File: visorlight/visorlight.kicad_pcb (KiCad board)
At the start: 2 copper layers, 85 x 35 mm, 3 parts, among them J1 Conn_01x04

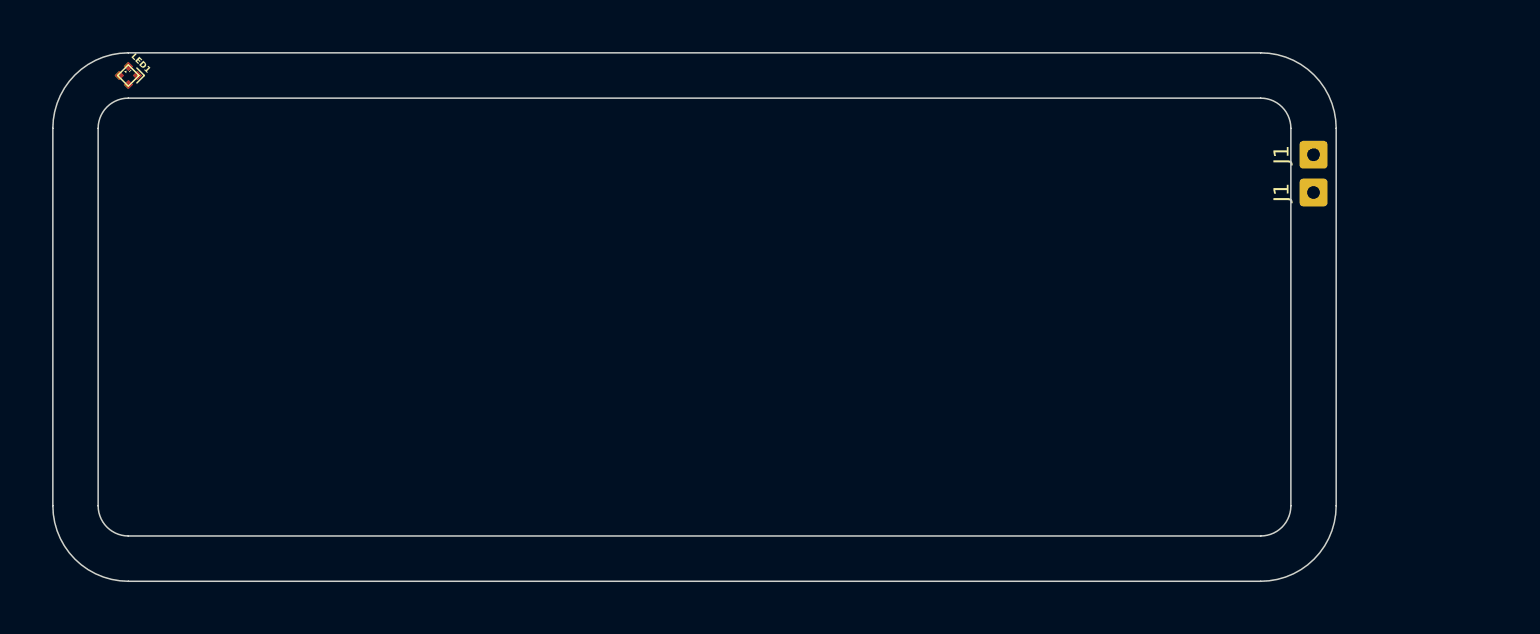
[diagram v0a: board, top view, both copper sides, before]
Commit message: moar leds
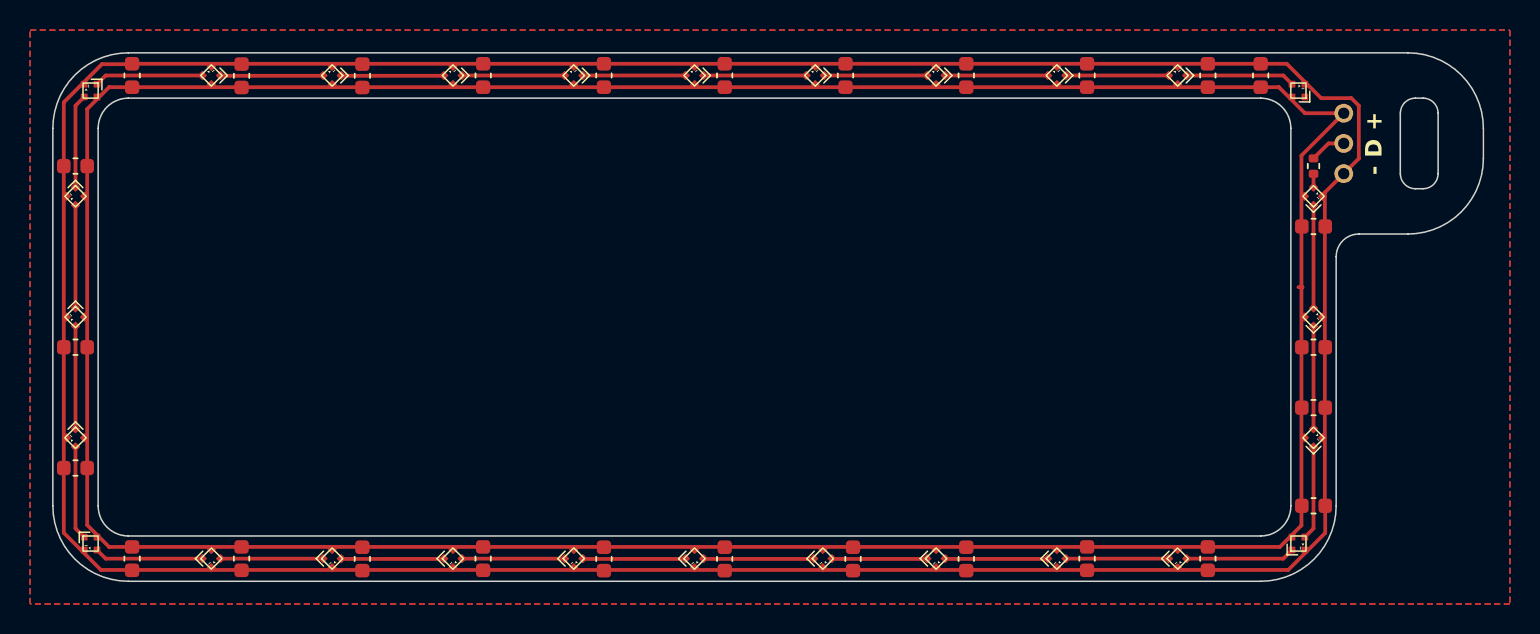
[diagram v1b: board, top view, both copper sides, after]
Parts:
- removed the J1 at (191.0, 89.2)
- removed the J1 at (191.0, 91.8)
- added C1: 0.1µF, Capacitor_SMD:C_0603_1608Metric, F.Cu at (191.0, 94.0)
- added C10: 0.1µF, Capacitor_SMD:C_0603_1608Metric, F.Cu at (144.0, 116.0)
- added C11: 0.1µF, Capacitor_SMD:C_0603_1608Metric, F.Cu at (136.0, 116.0)
- added C12: 0.1µF, Capacitor_SMD:C_0603_1608Metric, F.Cu at (128.0, 116.0)
- added C13: 0.1µF, Capacitor_SMD:C_0603_1608Metric, F.Cu at (120.0, 116.0)
- added C14: 0.1µF, Capacitor_SMD:C_0603_1608Metric, F.Cu at (112.8, 116.0)
- added C15: 0.1µF, Capacitor_SMD:C_0603_1608Metric, F.Cu at (109.0, 110.0)
- added C16: 0.1µF, Capacitor_SMD:C_0603_1608Metric, F.Cu at (109.0, 102.0)
- added C17: 0.1µF, Capacitor_SMD:C_0603_1608Metric, F.Cu at (109.0, 90.0)
- added C18: 0.1µF, Capacitor_SMD:C_0603_1608Metric, F.Cu at (112.8, 84.0)
- added C19: 0.1µF, Capacitor_SMD:C_0603_1608Metric, F.Cu at (120.0, 84.0)
- added C2: 0.1µF, Capacitor_SMD:C_0603_1608Metric, F.Cu at (191.0, 102.0)
- added C20: 0.1µF, Capacitor_SMD:C_0603_1608Metric, F.Cu at (128.0, 84.0)
- added C21: 0.1µF, Capacitor_SMD:C_0603_1608Metric, F.Cu at (136.0, 84.0)
- added C22: 0.1µF, Capacitor_SMD:C_0603_1608Metric, F.Cu at (144.0, 84.0)
- added C23: 0.1µF, Capacitor_SMD:C_0603_1608Metric, F.Cu at (152.0, 84.0)
- added C24: 0.1µF, Capacitor_SMD:C_0603_1608Metric, F.Cu at (160.0, 84.0)
- added C25: 0.1µF, Capacitor_SMD:C_0603_1608Metric, F.Cu at (168.0, 84.0)
- added C26: 0.1µF, Capacitor_SMD:C_0603_1608Metric, F.Cu at (176.0, 84.0)
- added C27: 0.1µF, Capacitor_SMD:C_0603_1608Metric, F.Cu at (184.0, 84.0)
- added C28: 0.1µF, Capacitor_SMD:C_0603_1608Metric, F.Cu at (187.5, 84.0)
- added C3: 0.1µF, Capacitor_SMD:C_0603_1608Metric, F.Cu at (191.0, 106.0)
- added C4: 0.1µF, Capacitor_SMD:C_0603_1608Metric, F.Cu at (191.0, 112.5)
- added C5: 0.1µF, Capacitor_SMD:C_0603_1608Metric, F.Cu at (184.0, 116.0)
- added C6: 0.1µF, Capacitor_SMD:C_0603_1608Metric, F.Cu at (176.0, 116.0)
- added C7: 0.1µF, Capacitor_SMD:C_0603_1608Metric, F.Cu at (168.0, 116.0)
- added C8: 0.1µF, Capacitor_SMD:C_0603_1608Metric, F.Cu at (160.5, 116.0)
- added C9: 0.1µF, Capacitor_SMD:C_0603_1608Metric, F.Cu at (152.0, 116.0)
- added J1: Conn_01x03, visorlight_parts:Wires_3x_Relief, F.Cu at (193.0, 88.5)
- added LED10: ~, visorlight_parts:LED_1010RGBC, F.Cu at (142.0, 116.0)
- added LED11: ~, visorlight_parts:LED_1010RGBC, F.Cu at (134.0, 116.0)
- added LED12: ~, visorlight_parts:LED_1010RGBC, F.Cu at (126.0, 116.0)
- added LED13: ~, visorlight_parts:LED_1010RGBC, F.Cu at (118.0, 116.0)
- added LED14: ~, visorlight_parts:LED_1010RGBC, F.Cu at (110.0, 115.0)
- added LED15: ~, visorlight_parts:LED_1010RGBC, F.Cu at (109.0, 108.0)
- added LED16: ~, visorlight_parts:LED_1010RGBC, F.Cu at (109.0, 100.0)
- added LED17: ~, visorlight_parts:LED_1010RGBC, F.Cu at (109.0, 92.0)
- added LED18: ~, visorlight_parts:LED_1010RGBC, F.Cu at (110.0, 85.0)
- added LED19: ~, visorlight_parts:LED_1010RGBC, F.Cu at (118.0, 84.0)
- added LED2: ~, visorlight_parts:LED_1010RGBC, F.Cu at (191.0, 100.0)
- added LED20: ~, visorlight_parts:LED_1010RGBC, F.Cu at (126.0, 84.0)
- added LED21: ~, visorlight_parts:LED_1010RGBC, F.Cu at (134.0, 84.0)
- added LED22: ~, visorlight_parts:LED_1010RGBC, F.Cu at (142.0, 84.0)
- added LED23: ~, visorlight_parts:LED_1010RGBC, F.Cu at (150.0, 84.0)
- added LED24: ~, visorlight_parts:LED_1010RGBC, F.Cu at (158.0, 84.0)
- added LED25: ~, visorlight_parts:LED_1010RGBC, F.Cu at (166.0, 84.0)
- added LED26: ~, visorlight_parts:LED_1010RGBC, F.Cu at (174.0, 84.0)
- added LED27: ~, visorlight_parts:LED_1010RGBC, F.Cu at (182.0, 84.0)
- added LED28: ~, visorlight_parts:LED_1010RGBC, F.Cu at (190.0, 85.0)
- added LED3: ~, visorlight_parts:LED_1010RGBC, F.Cu at (191.0, 108.0)
- added LED4: ~, visorlight_parts:LED_1010RGBC, F.Cu at (190.0, 115.0)
- added LED5: ~, visorlight_parts:LED_1010RGBC, F.Cu at (182.0, 116.0)
- added LED6: ~, visorlight_parts:LED_1010RGBC, F.Cu at (174.0, 116.0)
- added LED7: ~, visorlight_parts:LED_1010RGBC, F.Cu at (166.0, 116.0)
- added LED8: ~, visorlight_parts:LED_1010RGBC, F.Cu at (158.5, 116.0)
- added LED9: ~, visorlight_parts:LED_1010RGBC, F.Cu at (150.0, 116.0)
- added R1: 100Ω, Resistor_SMD:R_0402_1005Metric, F.Cu at (191.0, 90.0)
- LED1: footprint project_parts:LED_1010RGBC -> visorlight_parts:LED_1010RGBC
- moved LED1 78.9 mm to (191.0, 92.0), turned to 135 degrees
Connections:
- LED1 pad 1: unconnected-(LED1-DO-Pad1) -> Net-(LED1-DO)
- LED1 pad 2: unconnected-(LED1-VDD-Pad2) -> VDD
- LED1 pad 3: unconnected-(LED1-GND-Pad3) -> GND
- LED1 pad 4: unconnected-(LED1-DI-Pad4) -> Net-(LED1-DI)
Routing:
- net GND: track 0.00 -> 231.3 mm
- net VDD: track 0.00 -> 222.7 mm
- net Net-(LED8-DO): track 0.00 -> 7.31 mm
- net Net-(LED18-DO): track 0.00 -> 7.21 mm
- net Net-(LED13-DO): track 0.00 -> 7.21 mm
- net Net-(LED4-DO): track 0.00 -> 7.21 mm
- net Net-(LED27-DO): track 0.00 -> 7.21 mm
- net Net-(LED5-DO): track 0.00 -> 6.83 mm
- net Net-(LED21-DO): track 0.00 -> 6.83 mm
- net Net-(LED19-DO): track 0.00 -> 6.81 mm
- net Net-(LED20-DO): track 0.00 -> 6.81 mm
- net Net-(LED11-DO): track 0.00 -> 6.81 mm
- net Net-(LED6-DO): track 0.00 -> 6.81 mm
- net Net-(LED10-DI): track 0.00 -> 6.81 mm
- net Net-(LED2-DO): track 0.00 -> 6.80 mm
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- added copper zone on B.Cu, net GND
- added copper zone on F.Cu, net GND
- added copper zone on F.Cu, net VDD
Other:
- board size 85 x 35 mm -> 94.8 x 35 mm
